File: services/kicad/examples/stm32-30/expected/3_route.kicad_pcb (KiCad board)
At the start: 2 copper layers, 75 x 56.2 mm, 30 parts, among them J1 5V, U1 STM32F103C8T6, U2 AMS1117-3.3

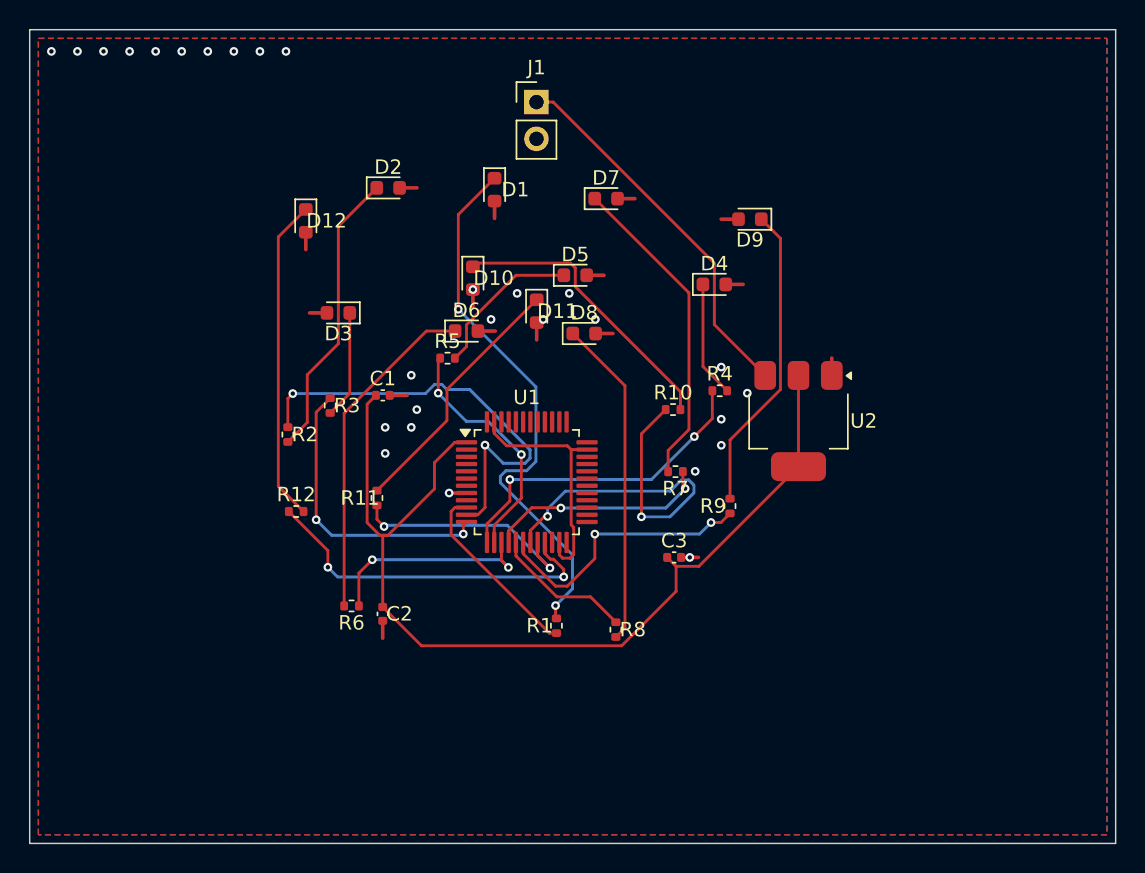
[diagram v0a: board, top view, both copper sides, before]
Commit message: feat(kicad): placement pro et routage 100 % fabricable sur les 16 cartes -- integration sur main (#164)
Branche d'integration coupee depuis origin/main (fab2a82, PR #162) : les
fichiers cles de main etaient des instantanes de feat/placement-seed-snap-
bypass (routing.py = 7981019, placement.py = 437a8b4...). On reprend donc
l'arbre entier de cette branche (345 commits, dernier 9f48667) et on y
conserve ce que main seul apportait :
- tools/verrou_routage.py + son test : « 6,2 Go par routage » rectifie
  (0,2 Go mesure ; c'est la concurrence qui emballe la memoire) ;
- tests/test_driver_llm_resync.py ;
- CLAUDE.md, PLAN.md, DECISIONS.md : fusion a trois voies, les sections
  des deux lignes conservees (2026-09-05 conteneur/verrou, 2026-09-07
  parcours asynchrone et chaine du driver, 2026-09-09/10 lecons).
Les skills *-delegate restent supprimes (remplaces le 2026-08-30).

Contenu : banc en deux phases (placement valide puis routage gele), snap
sur les regles natives, repli GND cible, journal Freerouting incremental,
horloge sans progres, via d'echappement vers le plan principal,
serigraphie degagee ; 16 cartes livrees a 100 %, 0 erreur DRC.

Verification : pytest services/kicad 1805 passed, 16 skipped ;
pnpm type-check 8/8.


Claude-Session: https://claude.ai/code/session_01TnMqm4La2CxQHHB5K8aSSV

Co-authored-by: Claude Fable 5.1 <noreply@anthropic.com>
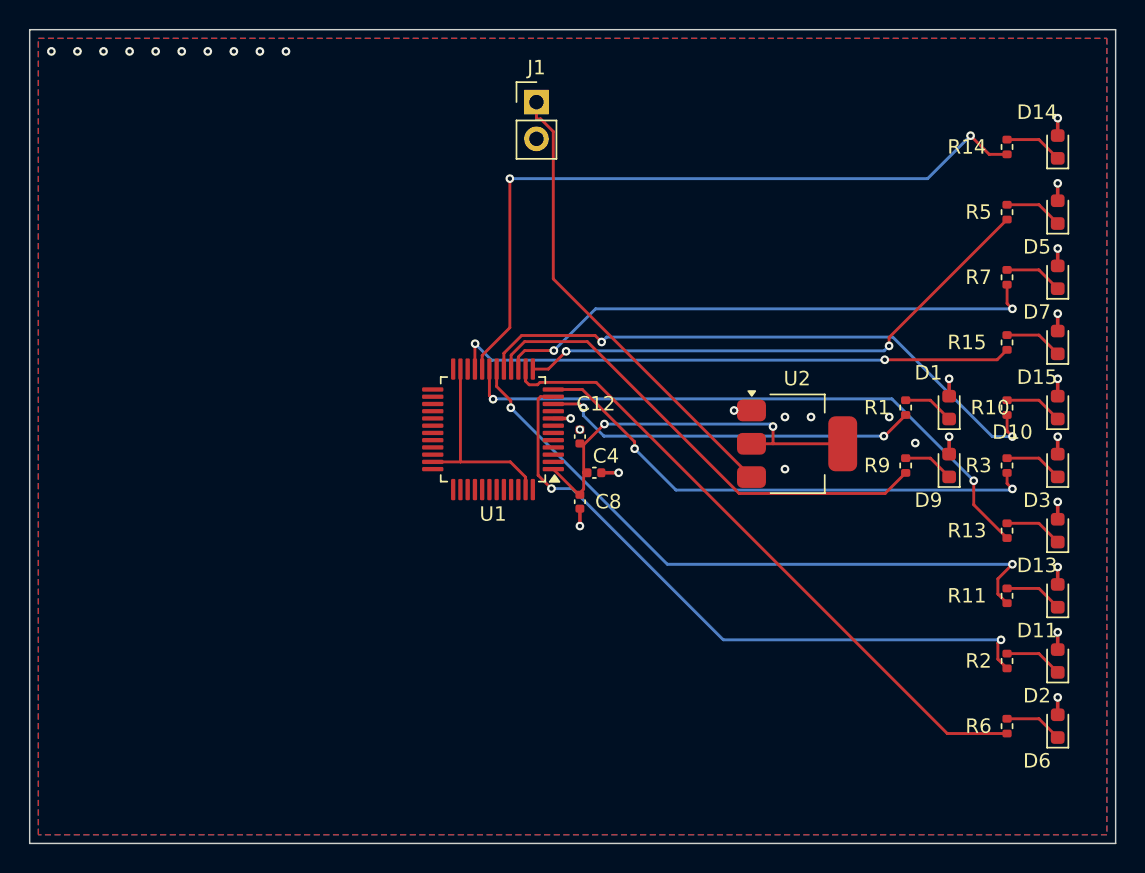
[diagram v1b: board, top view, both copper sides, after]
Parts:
- removed C1, C2, C3: 100nF, C_0402_1005Metric
- removed D12, D4, D8: LED, LED_0603_1608Metric
- removed R12, R4, R8: 330, R_0402_1005Metric
- added C12: 100nF, C_0402_1005Metric, F.Cu at (149.0, 105.0)
- added C4: 100nF, C_0402_1005Metric, F.Cu at (150.0, 107.5)
- added C8: 100nF, C_0402_1005Metric, F.Cu at (149.0, 109.5)
- added D13: LED, LED_0603_1608Metric, F.Cu at (182.0, 111.5)
- added D14: LED, LED_0603_1608Metric, F.Cu at (182.0, 85.0)
- added D15: LED, LED_0603_1608Metric, F.Cu at (182.0, 98.5)
- added R13: 330, R_0402_1005Metric, F.Cu at (178.5, 111.5)
- added R14: 330, R_0402_1005Metric, F.Cu at (178.5, 85.0)
- added R15: 330, R_0402_1005Metric, F.Cu at (178.5, 98.5)
- moved D2 56.6 mm to (182.0, 120.5), turned to 90 degrees
- moved R2 52.1 mm to (178.5, 120.5), turned to 90 degrees
- moved D3 50.8 mm to (182.0, 107.0), turned to 90 degrees
- moved D6 49.1 mm to (182.0, 125.0), turned to 90 degrees
- moved R3 46.9 mm to (178.5, 107.0), turned to 90 degrees
- moved R6 46.0 mm to (178.5, 125.0), turned to 90 degrees
- moved R11 44.0 mm to (178.5, 116.0)
- moved D10 41.4 mm to (182.0, 103.0), turned to 90 degrees
- moved D11 41.0 mm to (182.0, 116.0), turned to 90 degrees
- moved R5 39.9 mm to (178.5, 89.5), turned to 90 degrees
- moved D1 34.8 mm to (174.5, 103.0), turned to 90 degrees
- moved D5 33.6 mm to (182.0, 89.5), turned to 90 degrees
- moved D7 31.7 mm to (182.0, 94.0), turned to 90 degrees
- moved R1 28.4 mm to (171.5, 103.0)
- moved R7 26.5 mm to (178.5, 94.0), turned to 90 degrees
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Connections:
- D10 pad 1: LED13 -> LED10
- D11 pad 1: LED14 -> LED11
- D5 pad 1: LED6 -> LED5
- D6 pad 1: LED7 -> LED6
- D7 pad 1: LED9 -> LED7
- D9 pad 1: LED11 -> LED9
- R10 pad 1: GPIO13 -> GPIO10
- R10 pad 2: LED13 -> LED10
- R11 pad 1: GPIO14 -> GPIO11
- R11 pad 2: LED14 -> LED11
- R5 pad 1: GPIO6 -> GPIO5
- R5 pad 2: LED6 -> LED5
- R6 pad 1: GPIO7 -> GPIO6
- R6 pad 2: LED7 -> LED6
- R7 pad 1: GPIO9 -> GPIO7
- R7 pad 2: LED9 -> LED7
- R9 pad 1: GPIO11 -> GPIO9
- R9 pad 2: LED11 -> LED9
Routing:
- net +3V3: track 68.1 -> 27.9 mm, vias 0 -> 2
- net LED1: track 38.1 -> 3.54 mm, vias 2 -> 0
- net GPIO14: track 16.5 -> 50.0 mm
- net GPIO10: track 9.73 -> 41.5 mm, vias 0 -> 2
- net GPIO6: track 16.8 -> 44.3 mm, vias 2 -> 0
- net GPIO11: track 19.1 -> 45.6 mm
- net GPIO7: track 15.1 -> 38.2 mm
- net LED7: track 23.3 -> 4.04 mm
- net LED10: track 22.7 -> 4.04 mm
- net LED9: track 22.1 -> 3.54 mm
- net LED15: track 22.4 -> 4.04 mm
- net GPIO9: track 15.5 -> 33.5 mm, vias 2 -> 0
- net LED11: track 21.3 -> 4.04 mm
- net LED13: track 20.1 -> 4.04 mm
- net LED2: track 20.1 -> 4.04 mm
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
